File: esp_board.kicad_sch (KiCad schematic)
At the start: 2 parts, among them U1 ESP8285H16

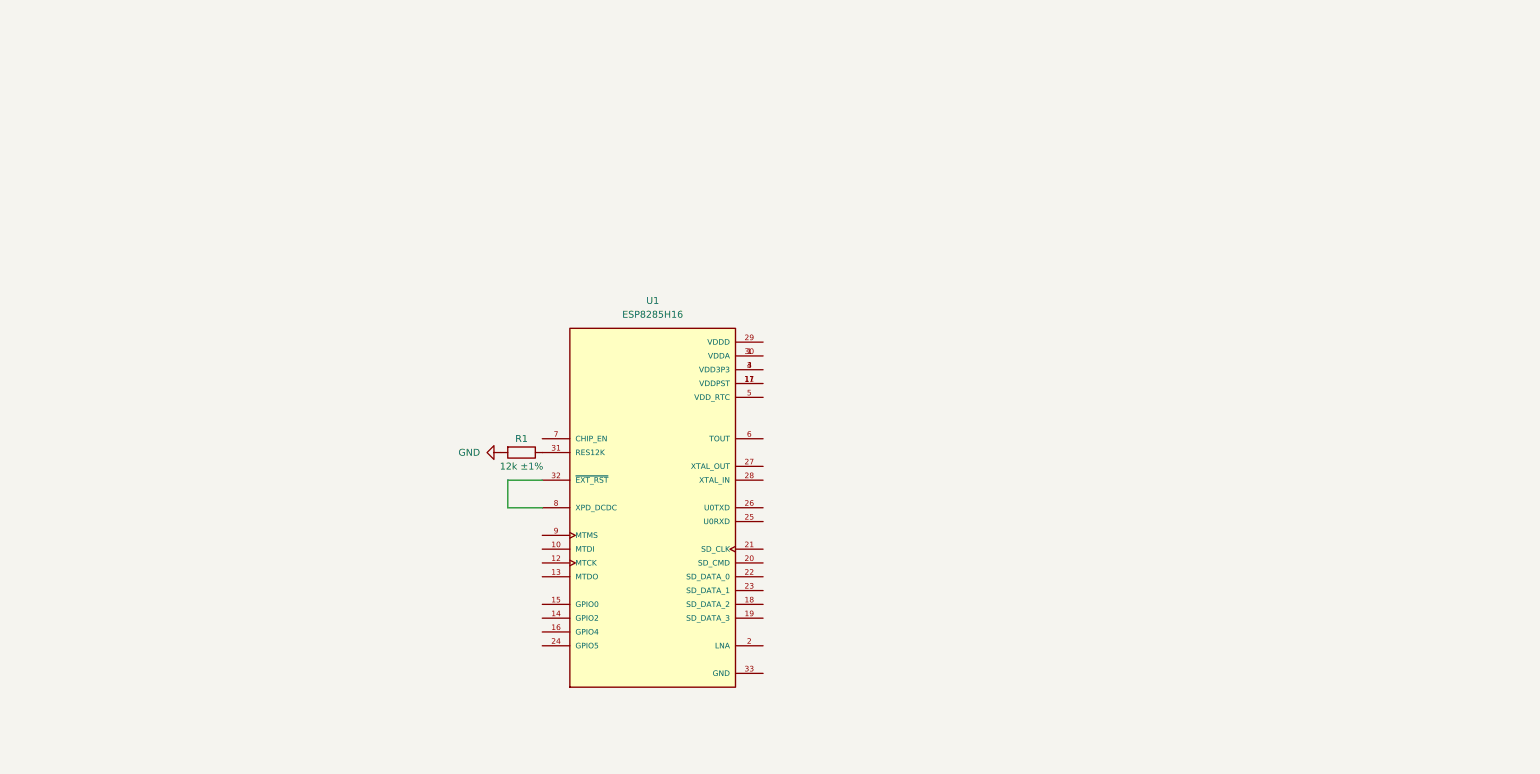
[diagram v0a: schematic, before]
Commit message: added sensor and power supply
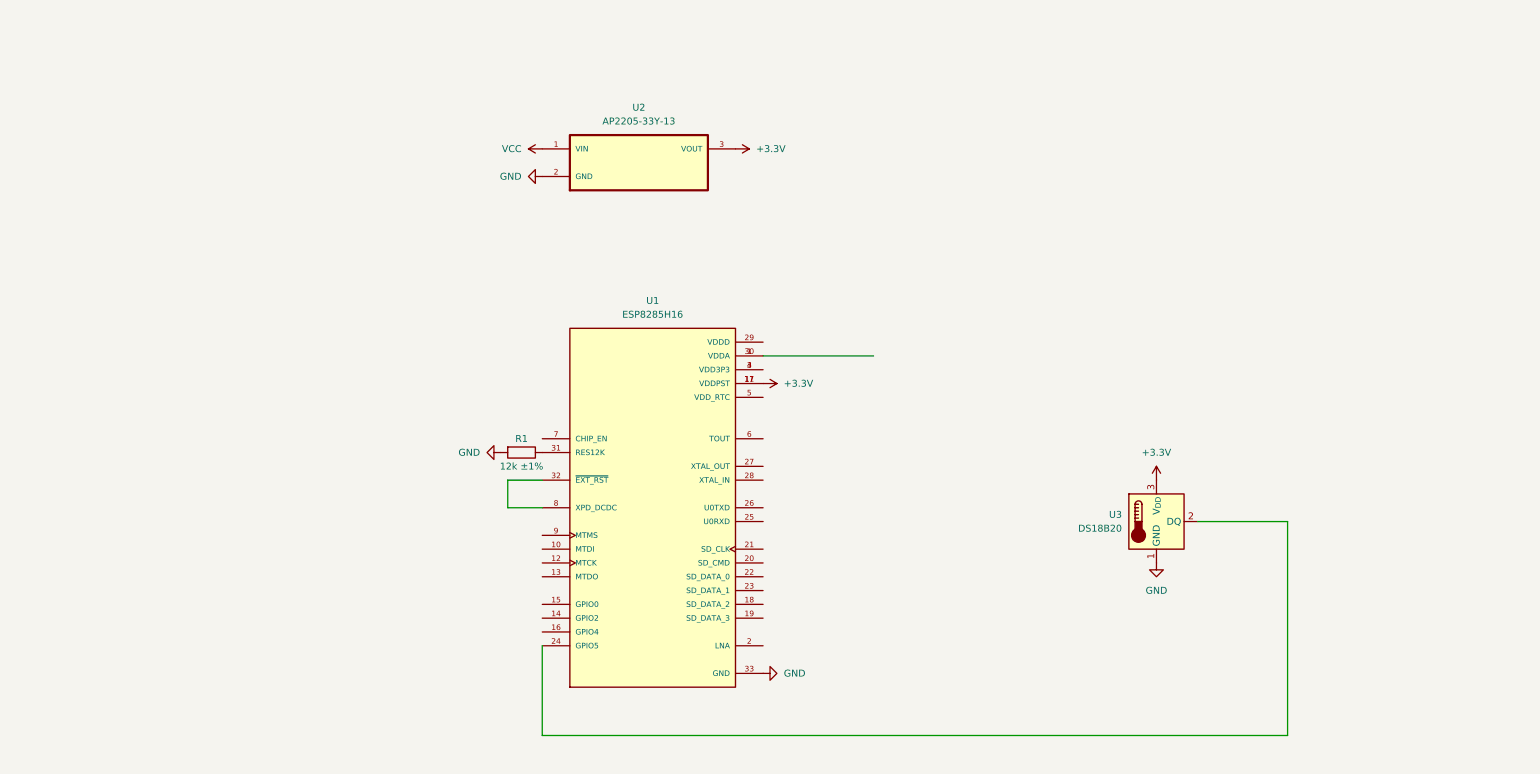
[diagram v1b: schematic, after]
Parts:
- added U2: AP2205-33Y-13, AP2205-33Y-13:VREG_AP7370-33Y-13, symbol custom:AP2205-33Y-13
- added U3: DS18B20, Package_TO_SOT_THT:TO-92_Inline, symbol Sensor_Temperature:DS18B20
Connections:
- net GND: now also U1.33 (GND), U2.2 (GND), U3.1 (GND)
- net +3.3V: now reaches U1.11 (VDDPST), U1.17 (VDDPST)
- net +3.3V: now also U2.3 (VOUT), U3.3 (V_{DD})
- net at U1.24 (GPIO5): now also U3.2 (DQ)
- new net VCC: U2.1 (VIN)

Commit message: changed footprint, worked on power supply
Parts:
- removed R1: 12k ±1%, symbol Device:R
- removed U1: ESP8285H16, ESP8285H16:QFN50P500X500X90-33N, symbol custom:ESP8285H16
- added C1: 1μF, symbol Device:C
- added C2: 1μF(NC), symbol Device:C
- added IC1: ESP8285, QFN50P500X500X90-33N-D, symbol custom:ESP8285
- added R2: 12k ±1%, symbol Device:R
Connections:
- net +3.3V: now also C1.1, C2.1, IC1.1 (VDDA_1), IC1.11 (VDDPST_1), IC1.17 (VDDPST_2), IC1.29 (VDDD), IC1.30 (VDDA_2)
- net GND: now also C1.2, C2.2, IC1.33 (EP), R2.2
- net at U3.2 (DQ): now also IC1.24 (GPIO5)
- new net: IC1.31 (RES12K), R2.1
- new net: IC1.32 (EXT_RSTB), IC1.8 (XDP_DCDC)

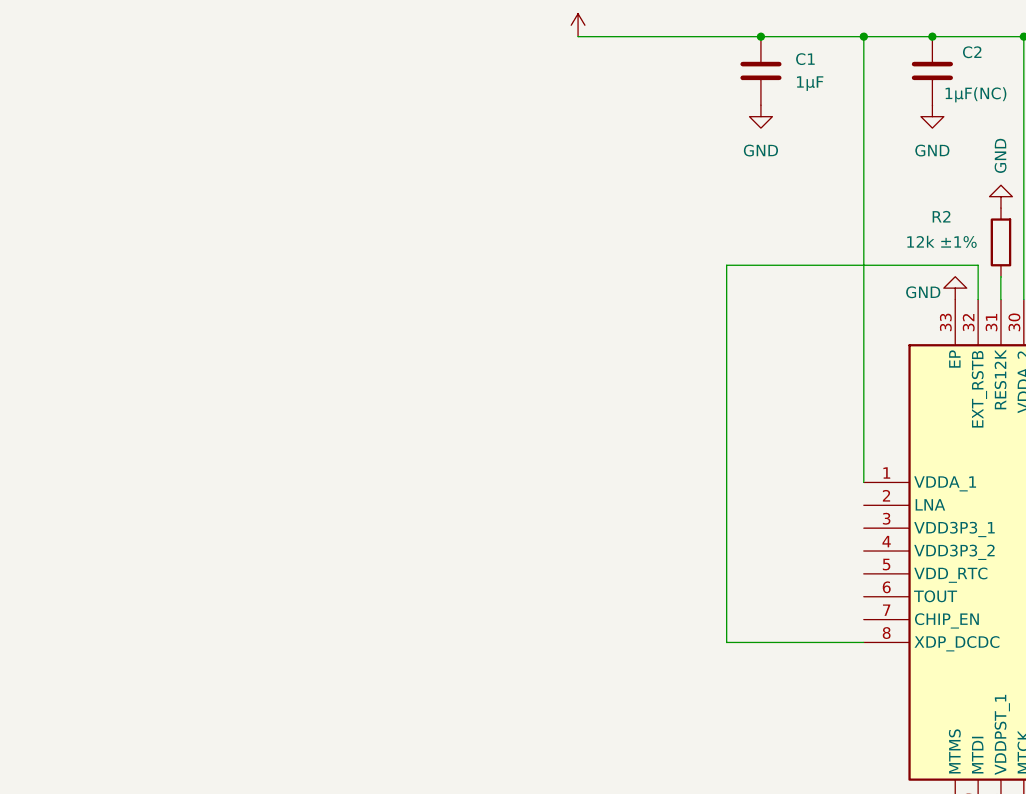
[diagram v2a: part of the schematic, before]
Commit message: added antenna
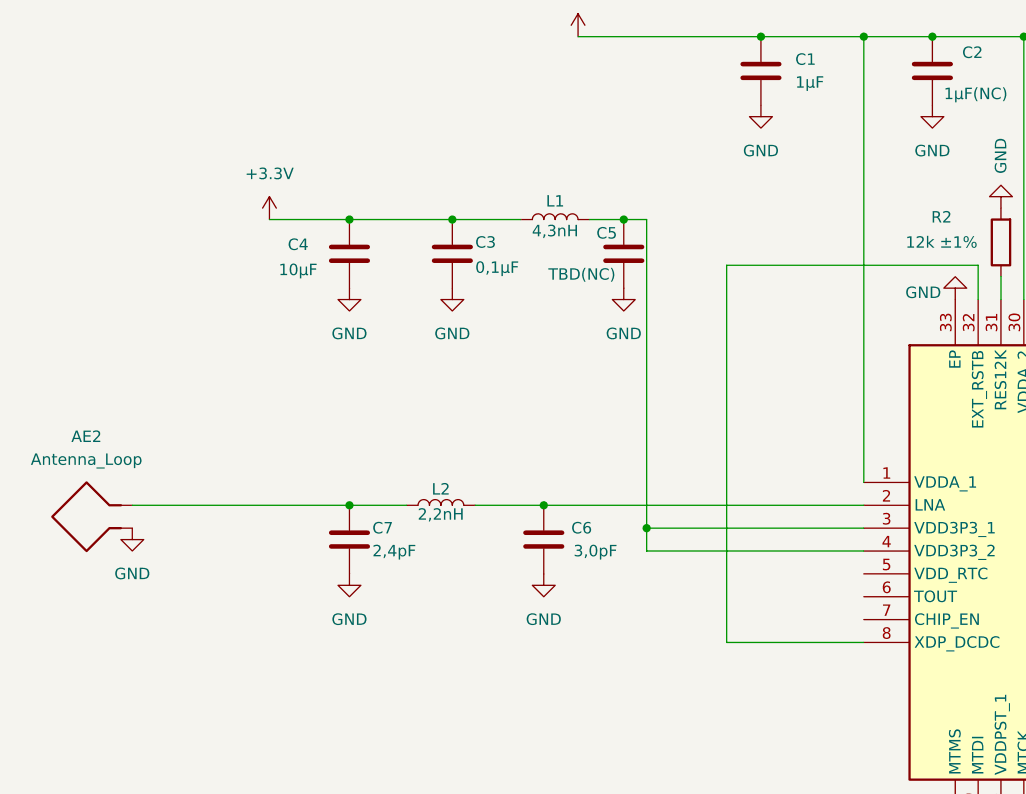
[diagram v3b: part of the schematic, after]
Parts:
- added AE2: Antenna_Loop, symbol Device:Antenna_Loop
- added C3: 0,1μF, symbol Device:C
- added C4: 10μF, symbol Device:C
- added C5: TBD(NC), symbol Device:C
- added C6: 3,0pF, symbol Device:C
- added C7: 2,4pF, symbol Device:C
- added L1: 4,3nH, symbol Device:L
- added L2: 2,2nH, symbol Device:L
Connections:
- net +3.3V: now also C3.1, C4.1, L1.1
- net GND: now also AE2.1, C3.2, C4.2, C5.2, C6.2, C7.2
- net at IC1.2 (LNA): now also C6.1, L2.2
- net at IC1.3 (VDD3P3_1): now also IC1.4 (VDD3P3_2), C5.1, L1.2
- new net: AE2.2, C7.1, L2.1

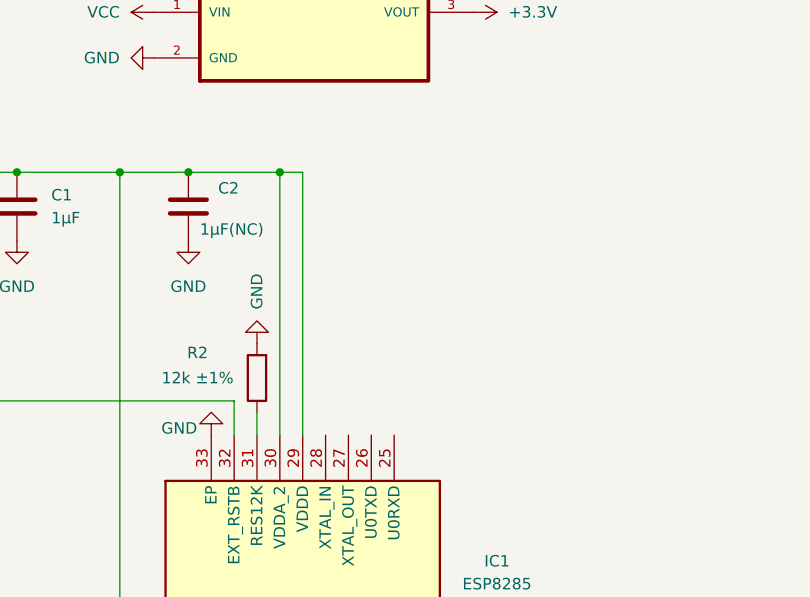
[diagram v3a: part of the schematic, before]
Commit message: added uart
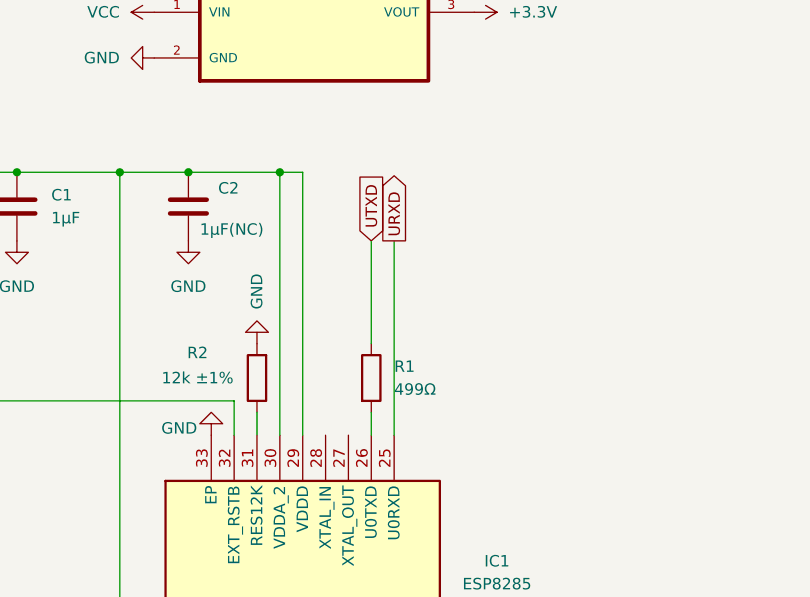
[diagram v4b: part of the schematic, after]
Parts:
- added R1: 499Ω, symbol Device:R
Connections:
- net URXD: now reaches IC1.25 (U0RXD)
- net at IC1.26 (U0TXD): now also R1.2
- new net UTXD: R1.1
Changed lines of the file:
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@@
+	(wire
+		(pts
+			(xy 153.67 74.93) (xy 153.67 77.47)
+		)
+		(stroke
+			(width 0)
+			(type default)
+		)
+	)
 	(wire
 		(pts
@@
 	(wire
 		(pts
+			(xy 153.67 55.88) (xy 153.67 67.31)
+		)
+		(stroke
+			(width 0)
+			(type default)
+		)
+	)
+	(wire
+		(pts
 			(xy 125.73 48.26) (xy 125.73 97.79)
 		)
@@
 	(wire
 		(pts
+			(xy 156.21 55.88) (xy 156.21 77.47)
+		)
+		(stroke
+			(width 0)
+			(type default)
+		)
+	)
+	(wire
+		(pts
 			(xy 166.37 97.79) (xy 213.36 97.79)
 		)
@@
 		)
 	)
+	(global_label "URXD"
+		(shape output)
+		(at 156.21 55.88 90)
+		(fields_autoplaced yes)
+		(effects
+			(font
+				(size 1.27 1.27)
+			)
+			(justify left)
+		)
+		(property "Intersheetrefs" "${INTERSHEET_REFS}"
+			(at 156.21 47.8148 90)
+			(effects
+				(font
+					(size 1.27 1.27)
+				)
+				(justify left)
+				(hide yes)
+			)
+		)
+	)
+	(global_label "UTXD"
+		(shape input)
+		(at 153.67 55.88 90)
+		(fields_autoplaced yes)
+		(effects
+			(font
+				(size 1.27 1.27)
+			)
+			(justify left)
+		)
+		(property "Intersheetrefs" "${INTERSHEET_REFS}"
+			(at 153.67 48.1172 90)
+			(effects
+				(font
+					(size 1.27 1.27)
+				)
+				(justify left)
+				(hide yes)
+			)
+		)
+	)
+	(symbol
+		(lib_id "Device:R")
+		(at 153.67 71.12 0)
+		(unit 1)
+		(exclude_from_sim no)
+		(in_bom yes)
+		(on_board yes)
+		(dnp no)
+		(fields_autoplaced yes)
+		(property "Reference" "R1"
+			(at 156.21 69.8499 0)
+			(effects
+				(font
+					(size 1.27 1.27)
+				)
+				(justify left)
+			)
+		)
+		(property "Value" "499Ω"
+			(at 156.21 72.3899 0)
+			(effects
+				(font
+					(size 1.27 1.27)
+				)
+				(justify left)
+			)
+		)
+		(property "Footprint" ""
+			(at 151.892 71.12 90)
+			(effects
+				(font
+					(size 1.27 1.27)
+				)
+				(hide yes)
+			)
+		)
+		(property "Datasheet" "~"
+			(at 153.67 71.12 0)
+			(effects
+				(font
+					(size 1.27 1.27)
+				)
+				(hide yes)
+			)
+		)
+		(property "Description" "Resistor"
+			(at 153.67 71.12 0)
+			(effects
+				(font
+					(size 1.27 1.27)
+				)
+				(hide yes)
+			)
+		)
+		(pin "1"
+		)
+		(pin "2"
+		)
+		(instances
+			(project "esp_board"
+				(path "/ee45c97c-cf60-4c2a-879f-17c11d9f0e29"
+					(reference "R1")
+					(unit 1)
+				)
+			)
+		)
+	)

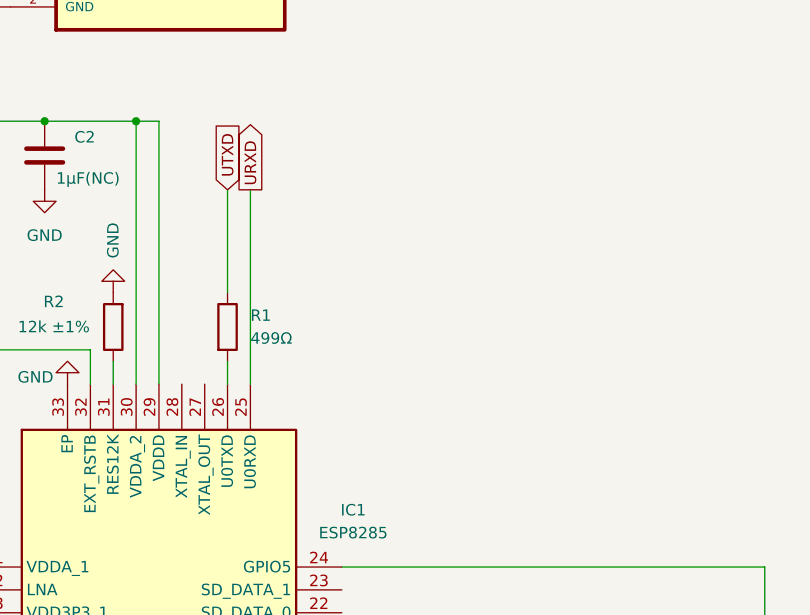
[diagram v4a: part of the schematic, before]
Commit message: added oscillator
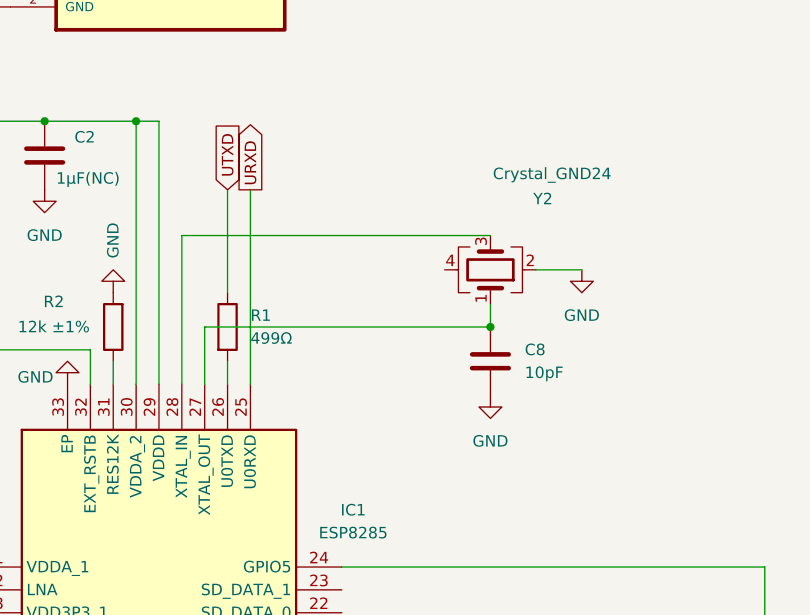
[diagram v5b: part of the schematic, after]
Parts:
- added C8: 10pF, symbol Device:C
- added Y2: Crystal_GND24, symbol Device:Crystal_GND24
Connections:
- net GND: now also C8.2, Y2.2
- net at IC1.27 (XTAL_OUT): now also C8.1, Y2.1
- net at IC1.28 (XTAL_IN): now also Y2.3
